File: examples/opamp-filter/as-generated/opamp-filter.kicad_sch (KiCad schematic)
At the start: 28 parts, among them J1 IN, J2 5V, J3 OUT, U1 MCP6001R, U2 MCP6001R

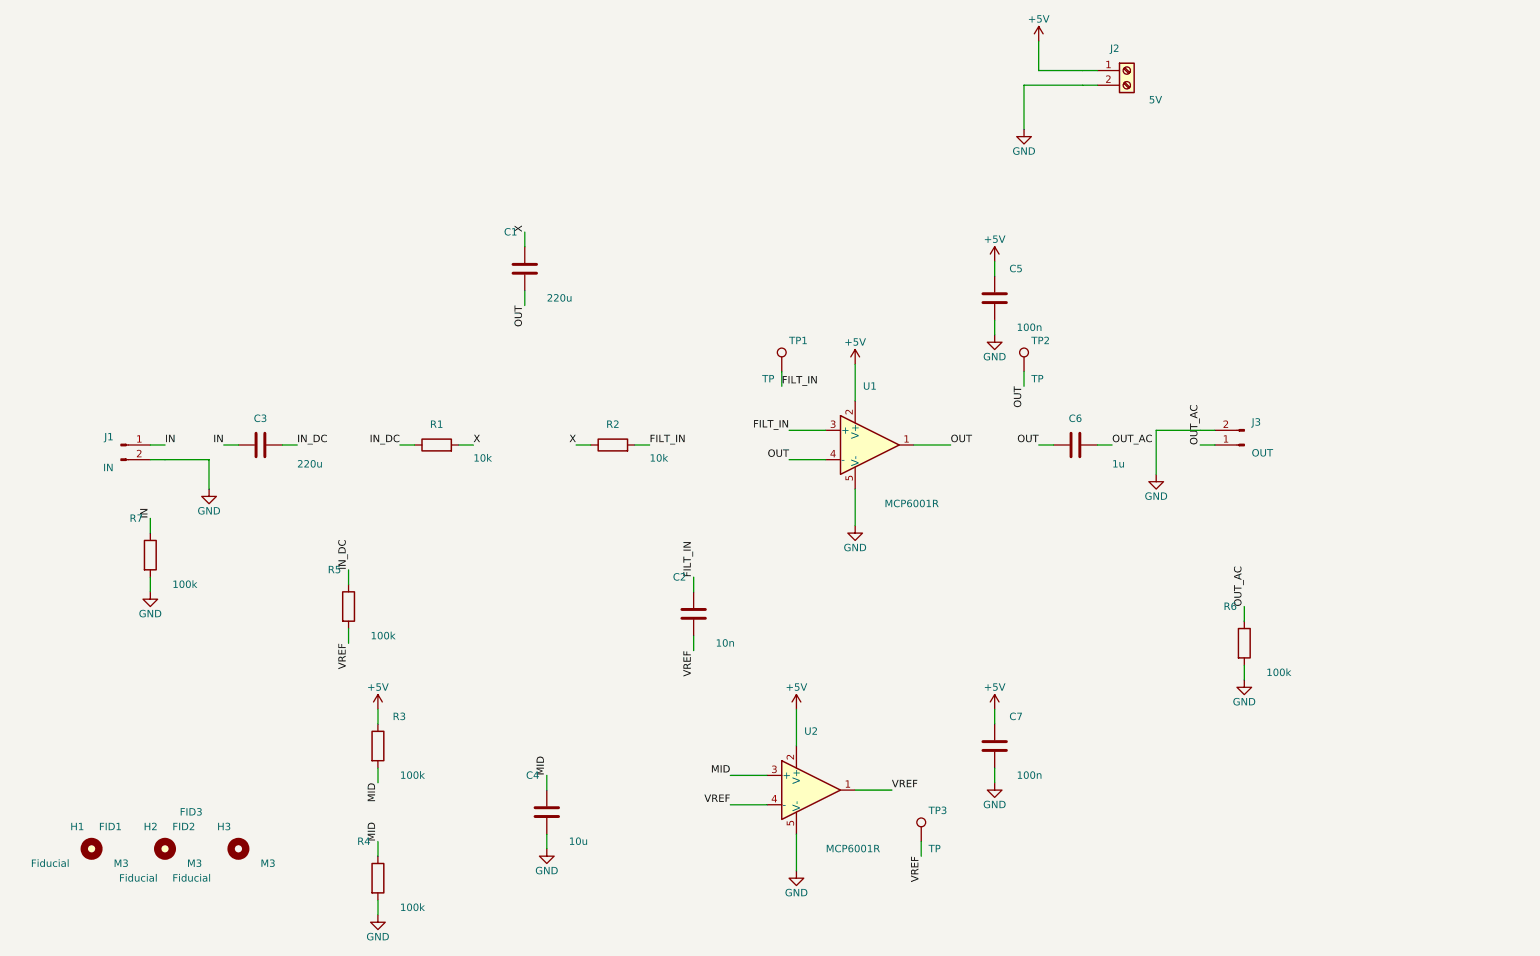
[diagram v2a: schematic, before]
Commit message: Let the new parts sit somewhere sensible, on the board and on the sheet
Placing screw holes and fiducials turned up four things that were wrong
before either existed, all of them about where something is allowed to
go rather than about the parts themselves.

A designator was kept off the pads but not inside the board outline, so
any part at the edge - a connector, and now a hole - had its reference
clipped by the edge. Every board had been carrying one or two of those.

A symbol with no pins leaves no trace in the sheet planner's obstacle
list, because that list is built from pin stubs. The screw holes were
invisible to it and the fiducials landed on top of them. The free-row
search also ran off the right-hand edge of an A4 page and sat over the
title block on the way, which is `readability.outside_page` and
`readability.margin_intrusion` respectively - both real, both now
avoided by bounding the search to the drawing area.

And the bill-of-materials flag is read from the footprint rather than
the symbol library, because the footprint is the side KiCad's parity
check reads and the side the fab agrees with. That retired three
warnings the op-amp board had been carrying since it gained test
points: `Connector:TestPoint` claims to be a BOM line and its own
footprint says otherwise.

All four fast boards pass their gates; the suite is green on 10.0.4.

Co-Authored-By: Claude Fable 5 <noreply@anthropic.com>
Claude-Session: https://claude.ai/code/session_01DUj7Ltu92tWg159mCSacwY
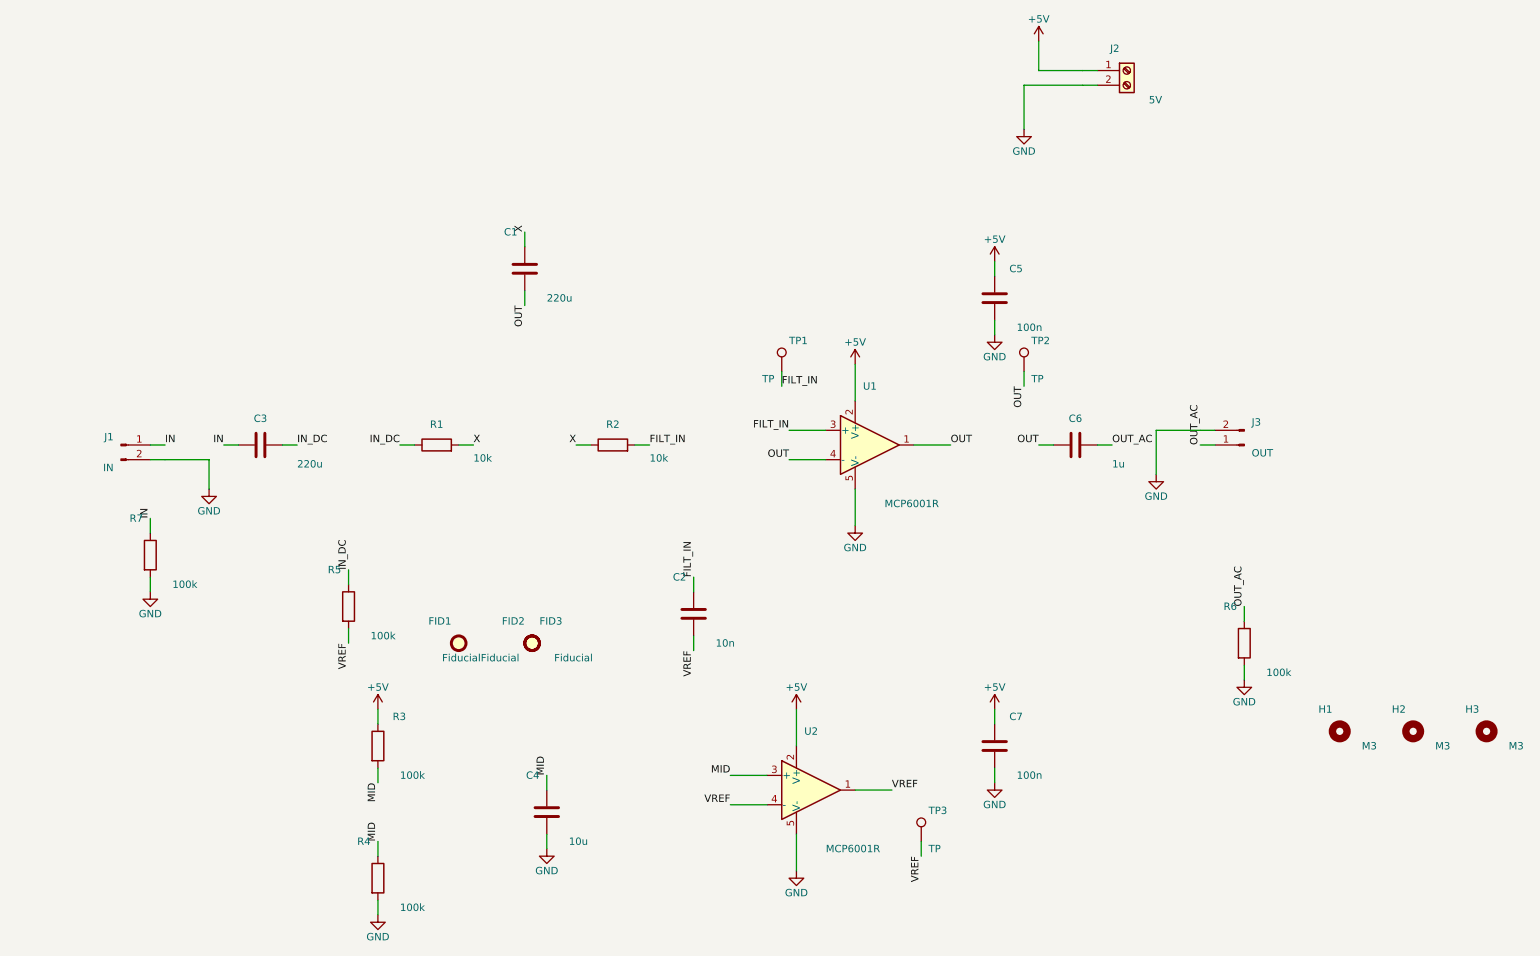
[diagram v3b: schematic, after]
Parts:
- FID1, FID2, FID3, H1, H2, H3, TP1, TP2, TP3: now left out of the parts list
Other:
- moved on the sheet: FID1, FID2, FID3, H1, H2, H3
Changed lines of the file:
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@@
   (label "FILT_IN" (at 145.09 89.98 0) (effects (font (size 1.27 1.27)) (justify left bottom)))
   (symbol (lib_id "Connector:TestPoint") (at 145.09 87.44 0.0) (unit 1)
-    (exclude_from_sim no) (in_bom yes) (on_board yes) (dnp no)
+    (exclude_from_sim no) (in_bom no) (on_board yes) (dnp no)
     (property "Reference" "TP1" (at 146.36 82.106 0) (effects (font (size 1.27 1.27)) (justify left)))
     (property "Value" "TP" (at 143.82 88.71 0) (effects (font (size 1.27 1.27)) (justify right)))
@@
   (label "OUT" (at 187.0 89.98 90) (effects (font (size 1.27 1.27)) (justify right bottom)))
   (symbol (lib_id "Connector:TestPoint") (at 187.0 87.44 0.0) (unit 1)
-    (exclude_from_sim no) (in_bom yes) (on_board yes) (dnp no)
+    (exclude_from_sim no) (in_bom no) (on_board yes) (dnp no)
     (property "Reference" "TP2" (at 188.27 82.106 0) (effects (font (size 1.27 1.27)) (justify left)))
     (property "Value" "TP" (at 188.27 88.71 0) (effects (font (size 1.27 1.27)) (justify left)))
@@
   (label "VREF" (at 169.22 171.26 90) (effects (font (size 1.27 1.27)) (justify right bottom)))
   (symbol (lib_id "Connector:TestPoint") (at 169.22 168.72 0.0) (unit 1)
-    (exclude_from_sim no) (in_bom yes) (on_board yes) (dnp no)
+    (exclude_from_sim no) (in_bom no) (on_board yes) (dnp no)
     (property "Reference" "TP3" (at 170.49 163.386 0) (effects (font (size 1.27 1.27)) (justify left)))
     (property "Value" "TP" (at 170.49 169.99 0) (effects (font (size 1.27 1.27)) (justify left)))
@@
     (instances (project "opamp-filter" (path "/efb028ab-a5b5-5d27-b654-08a8ba6b5d9d" (reference "TP3") (unit 1))))
   )
-  (symbol (lib_id "Mechanical:MountingHole") (at 25.71 169.99 0.0) (unit 1)
-    (exclude_from_sim no) (in_bom yes) (on_board yes) (dnp no)
-    (property "Reference" "H1" (at 24.44 166.18 0) (effects (font (size 1.27 1.27)) (justify right)))
-    (property "Value" "M3" (at 29.52 172.53 0) (effects (font (size 1.27 1.27)) (justify left)))
-    (property "Footprint" "MountingHole:MountingHole_3.2mm_M3" (at 25.71 169.99 0) (effects (font (size 1.27 1.27)) hide))
-    (property "Datasheet" "~" (at 25.71 169.99 0) (effects (font (size 1.27 1.27)) hide))
+  (symbol (lib_id "Mechanical:MountingHole") (at 241.61 149.67 0.0) (unit 1)
+    (exclude_from_sim no) (in_bom no) (on_board yes) (dnp no)
+    (property "Reference" "H1" (at 240.34 145.86 0) (effects (font (size 1.27 1.27)) (justify right)))
+    (property "Value" "M3" (at 245.42 152.21 0) (effects (font (size 1.27 1.27)) (justify left)))
+    (property "Footprint" "MountingHole:MountingHole_3.2mm_M3" (at 241.61 149.67 0) (effects (font (size 1.27 1.27)) hide))
+    (property "Datasheet" "~" (at 241.61 149.67 0) (effects (font (size 1.27 1.27)) hide))
     (instances (project "opamp-filter" (path "/efb028ab-a5b5-5d27-b654-08a8ba6b5d9d" (reference "H1") (unit 1))))
   )
-  (symbol (lib_id "Mechanical:MountingHole") (at 38.41 169.99 0.0) (unit 1)
-    (exclude_from_sim no) (in_bom yes) (on_board yes) (dnp no)
-    (property "Reference" "H2" (at 37.14 166.18 0) (effects (font (size 1.27 1.27)) (justify right)))
-    (property "Value" "M3" (at 42.22 172.53 0) (effects (font (size 1.27 1.27)) (justify left)))
-    (property "Footprint" "MountingHole:MountingHole_3.2mm_M3" (at 38.41 169.99 0) (effects (font (size 1.27 1.27)) hide))
-    (property "Datasheet" "~" (at 38.41 169.99 0) (effects (font (size 1.27 1.27)) hide))
+  (symbol (lib_id "Mechanical:MountingHole") (at 254.31 149.67 0.0) (unit 1)
+    (exclude_from_sim no) (in_bom no) (on_board yes) (dnp no)
+    (property "Reference" "H2" (at 253.04 145.86 0) (effects (font (size 1.27 1.27)) (justify right)))
+    (property "Value" "M3" (at 258.12 152.21 0) (effects (font (size 1.27 1.27)) (justify left)))
+    (property "Footprint" "MountingHole:MountingHole_3.2mm_M3" (at 254.31 149.67 0) (effects (font (size 1.27 1.27)) hide))
+    (property "Datasheet" "~" (at 254.31 149.67 0) (effects (font (size 1.27 1.27)) hide))
     (instances (project "opamp-filter" (path "/efb028ab-a5b5-5d27-b654-08a8ba6b5d9d" (reference "H2") (unit 1))))
   )
-  (symbol (lib_id "Mechanical:MountingHole") (at 51.11 169.99 0.0) (unit 1)
-    (exclude_from_sim no) (in_bom yes) (on_board yes) (dnp no)
-    (property "Reference" "H3" (at 49.84 166.18 0) (effects (font (size 1.27 1.27)) (justify right)))
-    (property "Value" "M3" (at 54.92 172.53 0) (effects (font (size 1.27 1.27)) (justify left)))
-    (property "Footprint" "MountingHole:MountingHole_3.2mm_M3" (at 51.11 169.99 0) (effects (font (size 1.27 1.27)) hide))
-    (property "Datasheet" "~" (at 51.11 169.99 0) (effects (font (size 1.27 1.27)) hide))
+  (symbol (lib_id "Mechanical:MountingHole") (at 267.01 149.67 0.0) (unit 1)
+    (exclude_from_sim no) (in_bom no) (on_board yes) (dnp no)
+    (property "Reference" "H3" (at 265.74 145.86 0) (effects (font (size 1.27 1.27)) (justify right)))
+    (property "Value" "M3" (at 270.82 152.21 0) (effects (font (size 1.27 1.27)) (justify left)))
+    (property "Footprint" "MountingHole:MountingHole_3.2mm_M3" (at 267.01 149.67 0) (effects (font (size 1.27 1.27)) hide))
+    (property "Datasheet" "~" (at 267.01 149.67 0) (effects (font (size 1.27 1.27)) hide))
     (instances (project "opamp-filter" (path "/efb028ab-a5b5-5d27-b654-08a8ba6b5d9d" (reference "H3") (unit 1))))
   )
-  (symbol (lib_id "Mechanical:Fiducial") (at 25.71 169.99 0.0) (unit 1)
-    (exclude_from_sim no) (in_bom yes) (on_board yes) (dnp no)
-    (property "Reference" "FID1" (at 26.98 166.18 0) (effects (font (size 1.27 1.27)) (justify left)))
-    (property "Value" "Fiducial" (at 21.9 172.53 0) (effects (font (size 1.27 1.27)) (justify right)))
-    (property "Footprint" "Fiducial:Fiducial_1mm_Mask2mm" (at 25.71 169.99 0) (effects (font (size 1.27 1.27)) hide))
-    (property "Datasheet" "~" (at 25.71 169.99 0) (effects (font (size 1.27 1.27)) hide))
+  (symbol (lib_id "Mechanical:Fiducial") (at 89.21 134.43 0.0) (unit 1)
+    (exclude_from_sim no) (in_bom no) (on_board yes) (dnp no)
+    (property "Reference" "FID1" (at 87.94 130.62 0) (effects (font (size 1.27 1.27)) (justify right)))
+    (property "Value" "Fiducial" (at 93.02 136.97 0) (effects (font (size 1.27 1.27)) (justify left)))
+    (property "Footprint" "Fiducial:Fiducial_1mm_Mask2mm" (at 89.21 134.43 0) (effects (font (size 1.27 1.27)) hide))
+    (property "Datasheet" "~" (at 89.21 134.43 0) (effects (font (size 1.27 1.27)) hide))
     (instances (project "opamp-filter" (path "/efb028ab-a5b5-5d27-b654-08a8ba6b5d9d" (reference "FID1") (unit 1))))
   )
-  (symbol (lib_id "Mechanical:Fiducial") (at 38.41 169.99 0.0) (unit 1)
-    (exclude_from_sim no) (in_bom yes) (on_board yes) (dnp no)
-    (property "Reference" "FID2" (at 39.68 166.18 0) (effects (font (size 1.27 1.27)) (justify left)))
-    (property "Value" "Fiducial" (at 39.68 175.07 0) (effects (font (size 1.27 1.27)) (justify left)))
-    (property "Footprint" "Fiducial:Fiducial_1mm_Mask2mm" (at 38.41 169.99 0) (effects (font (size 1.27 1.27)) hide))
-    (property "Datasheet" "~" (at 38.41 169.99 0) (effects (font (size 1.27 1.27)) hide))
+  (symbol (lib_id "Mechanical:Fiducial") (at 101.91 134.43 0.0) (unit 1)
+    (exclude_from_sim no) (in_bom no) (on_board yes) (dnp no)
+    (property "Reference" "FID2" (at 100.64 130.62 0) (effects (font (size 1.27 1.27)) (justify right)))
+    (property "Value" "Fiducial" (at 105.72 136.97 0) (effects (font (size 1.27 1.27)) (justify left)))
+    (property "Footprint" "Fiducial:Fiducial_1mm_Mask2mm" (at 101.91 134.43 0) (effects (font (size 1.27 1.27)) hide))
+    (property "Datasheet" "~" (at 101.91 134.43 0) (effects (font (size 1.27 1.27)) hide))
     (instances (project "opamp-filter" (path "/efb028ab-a5b5-5d27-b654-08a8ba6b5d9d" (reference "FID2") (unit 1))))
   )
-  (symbol (lib_id "Mechanical:Fiducial") (at 38.41 169.99 0.0) (unit 1)
-    (exclude_from_sim no) (in_bom yes) (on_board yes) (dnp no)
-    (property "Reference" "FID3" (at 40.95 163.64 0) (effects (font (size 1.27 1.27)) (justify left)))
-    (property "Value" "Fiducial" (at 37.14 175.07 0) (effects (font (size 1.27 1.27)) (justify right)))
-    (property "Footprint" "Fiducial:Fiducial_1mm_Mask2mm" (at 38.41 169.99 0) (effects (font (size 1.27 1.27)) hide))
-    (property "Datasheet" "~" (at 38.41 169.99 0) (effects (font (size 1.27 1.27)) hide))
+  (symbol (lib_id "Mechanical:Fiducial") (at 101.91 134.43 0.0) (unit 1)
+    (exclude_from_sim no) (in_bom no) (on_board yes) (dnp no)
+    (property "Reference" "FID3" (at 103.18 130.62 0) (effects (font (size 1.27 1.27)) (justify left)))
+    (property "Value" "Fiducial" (at 93.02 136.97 0) (effects (font (size 1.27 1.27)) (justify right)))
+    (property "Footprint" "Fiducial:Fiducial_1mm_Mask2mm" (at 101.91 134.43 0) (effects (font (size 1.27 1.27)) hide))
+    (property "Datasheet" "~" (at 101.91 134.43 0) (effects (font (size 1.27 1.27)) hide))
     (instances (project "opamp-filter" (path "/efb028ab-a5b5-5d27-b654-08a8ba6b5d9d" (reference "FID3") (unit 1))))
   )

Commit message: Put the vias back where the copper moved, and let the fillets vote
The FPGA board came back from its re-route with two unconnected nets and
three dangling ends, and the cause was older than anything this round
added. The router hands back a via for every layer change; six passes
then reshape the copper - snapping to 45s, chamfering, spreading folds,
and now filleting - and none of them move the holes underneath. A joint
that slides a millimetre from its via is two loose ends and one broken
net, and `_unlooped` then swept the via away as orphaned, because it
kept a via only when a track ended on its exact coordinate.

Two fixes, both about what "connected" means. A via lives if kept copper
*touches* it, not if a coordinate matches. And a new `_joined` pass
re-derives the joints from the copper that actually got written: where a
net ends on two layers at one point with no via reaching it, one goes
back in. It reads the finished geometry, so it cannot drift the way six
separate passes carrying vias along with them would.

The same reasoning fixes two rules that had been measuring coordinates
rather than copper. `route.stub` matched a track end to a via's centre
exactly, and called a joint a stub whenever a reshaping pass had moved
it a quarter of a millimetre inside the very barrel it was connected to.
`route.width_step` walked a neck back to its pad and stopped at the
first width change - which, on a filleted board, is the teardrop, so
every escape's neck stopped being recognised as one.

While the three copies of the post-route pipeline were being edited for
the third time this session, they became one function. That is how
`_teardrops` had come to run on two of the three exits.

All five boards: DRC clean on both matrix versions, nothing unconnected.
Four pass their gates; the FPGA board is down to the two-layer bill it
has always had - four nets over plane cuts and one 88 degree corner.

Co-Authored-By: Claude Fable 5 <noreply@anthropic.com>
Claude-Session: https:/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
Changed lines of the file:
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@@
     (exclude_from_sim no) (in_bom no) (on_board yes) (dnp no)
     (property "Reference" "H1" (at 240.34 145.86 0) (effects (font (size 1.27 1.27)) (justify right)))
-    (property "Value" "M3" (at 245.42 152.21 0) (effects (font (size 1.27 1.27)) (justify left)))
+    (property "Value" "M3" (at 245.42 152.21 0) (effects (font (size 1.27 1.27)) (justify left) hide))
     (property "Footprint" "MountingHole:MountingHole_3.2mm_M3" (at 241.61 149.67 0) (effects (font (size 1.27 1.27)) hide))
     (property "Datasheet" "~" (at 241.61 149.67 0) (effects (font (size 1.27 1.27)) hide))
@@
     (exclude_from_sim no) (in_bom no) (on_board yes) (dnp no)
     (property "Reference" "H2" (at 253.04 145.86 0) (effects (font (size 1.27 1.27)) (justify right)))
-    (property "Value" "M3" (at 258.12 152.21 0) (effects (font (size 1.27 1.27)) (justify left)))
+    (property "Value" "M3" (at 258.12 152.21 0) (effects (font (size 1.27 1.27)) (justify left) hide))
     (property "Footprint" "MountingHole:MountingHole_3.2mm_M3" (at 254.31 149.67 0) (effects (font (size 1.27 1.27)) hide))
     (property "Datasheet" "~" (at 254.31 149.67 0) (effects (font (size 1.27 1.27)) hide))
@@
     (exclude_from_sim no) (in_bom no) (on_board yes) (dnp no)
     (property "Reference" "H3" (at 265.74 145.86 0) (effects (font (size 1.27 1.27)) (justify right)))
-    (property "Value" "M3" (at 270.82 152.21 0) (effects (font (size 1.27 1.27)) (justify left)))
+    (property "Value" "M3" (at 270.82 152.21 0) (effects (font (size 1.27 1.27)) (justify left) hide))
     (property "Footprint" "MountingHole:MountingHole_3.2mm_M3" (at 267.01 149.67 0) (effects (font (size 1.27 1.27)) hide))
     (property "Datasheet" "~" (at 267.01 149.67 0) (effects (font (size 1.27 1.27)) hide))
@@
     (exclude_from_sim no) (in_bom no) (on_board yes) (dnp no)
     (property "Reference" "FID1" (at 87.94 130.62 0) (effects (font (size 1.27 1.27)) (justify right)))
-    (property "Value" "Fiducial" (at 93.02 136.97 0) (effects (font (size 1.27 1.27)) (justify left)))
+    (property "Value" "Fiducial" (at 93.02 136.97 0) (effects (font (size 1.27 1.27)) (justify left) hide))
     (property "Footprint" "Fiducial:Fiducial_1mm_Mask2mm" (at 89.21 134.43 0) (effects (font (size 1.27 1.27)) hide))
     (property "Datasheet" "~" (at 89.21 134.43 0) (effects (font (size 1.27 1.27)) hide))
@@
     (exclude_from_sim no) (in_bom no) (on_board yes) (dnp no)
     (property "Reference" "FID2" (at 100.64 130.62 0) (effects (font (size 1.27 1.27)) (justify right)))
-    (property "Value" "Fiducial" (at 105.72 136.97 0) (effects (font (size 1.27 1.27)) (justify left)))
+    (property "Value" "Fiducial" (at 105.72 136.97 0) (effects (font (size 1.27 1.27)) (justify left) hide))
     (property "Footprint" "Fiducial:Fiducial_1mm_Mask2mm" (at 101.91 134.43 0) (effects (font (size 1.27 1.27)) hide))
     (property "Datasheet" "~" (at 101.91 134.43 0) (effects (font (size 1.27 1.27)) hide))
@@
     (exclude_from_sim no) (in_bom no) (on_board yes) (dnp no)
     (property "Reference" "FID3" (at 103.18 130.62 0) (effects (font (size 1.27 1.27)) (justify left)))
-    (property "Value" "Fiducial" (at 93.02 136.97 0) (effects (font (size 1.27 1.27)) (justify right)))
+    (property "Value" "Fiducial" (at 93.02 136.97 0) (effects (font (size 1.27 1.27)) (justify right) hide))
     (property "Footprint" "Fiducial:Fiducial_1mm_Mask2mm" (at 101.91 134.43 0) (effects (font (size 1.27 1.27)) hide))
     (property "Datasheet" "~" (at 101.91 134.43 0) (effects (font (size 1.27 1.27)) hide))
